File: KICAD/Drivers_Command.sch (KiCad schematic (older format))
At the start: 12 parts

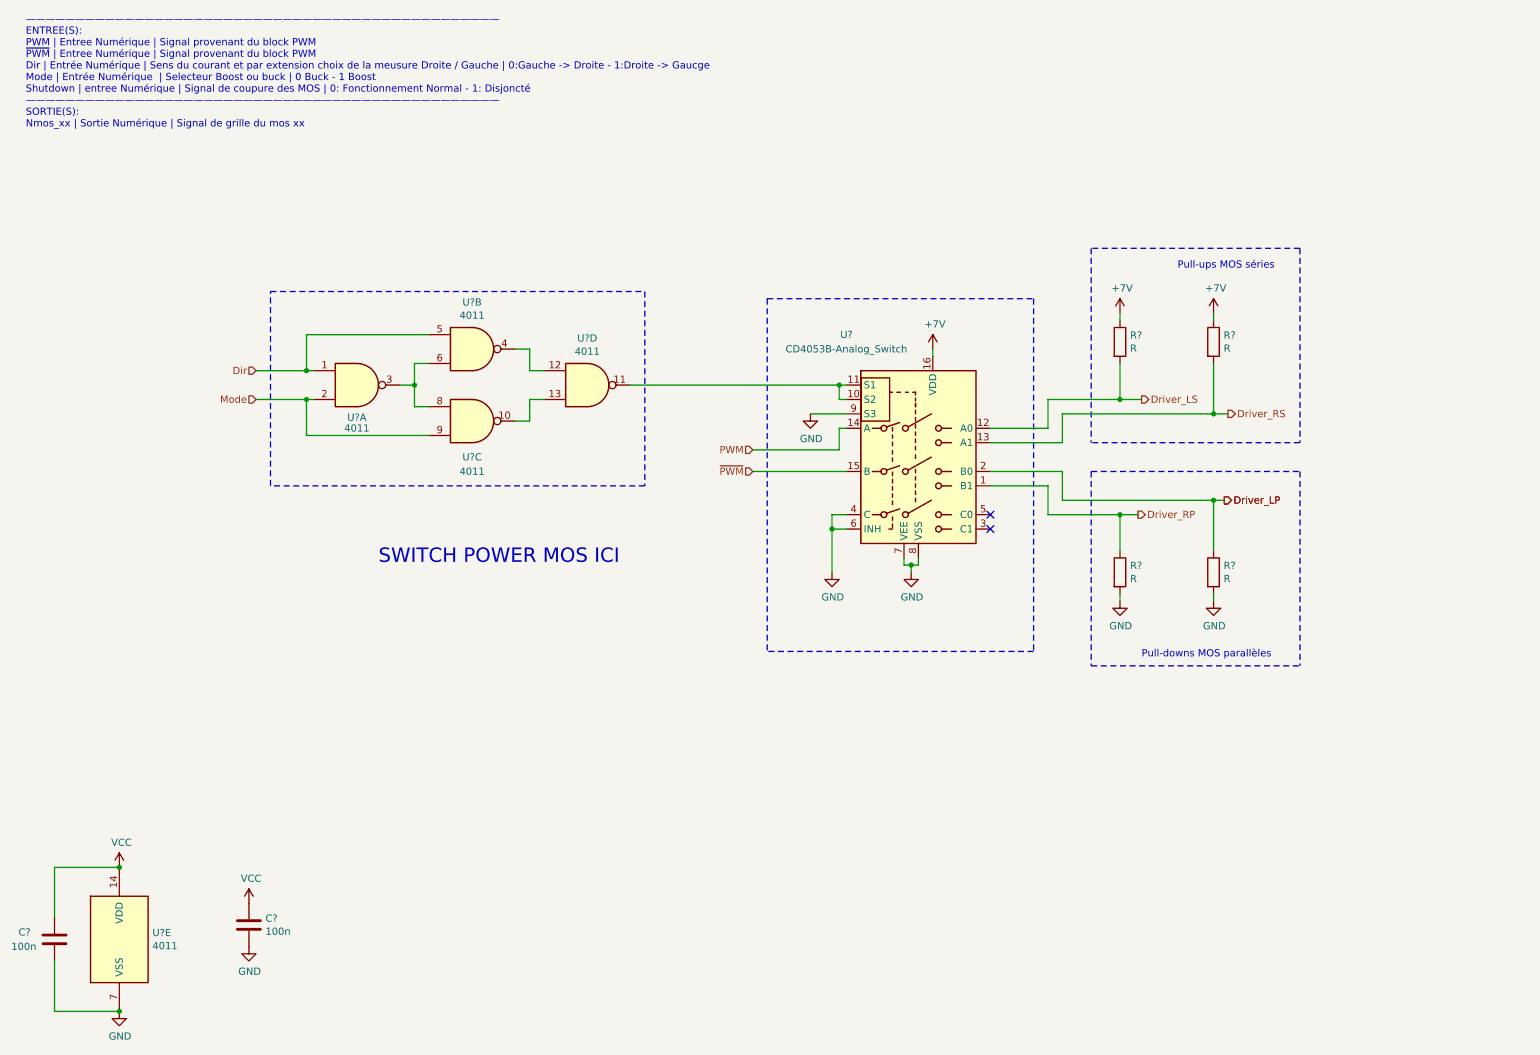
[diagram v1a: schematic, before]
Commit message: reworked driver command
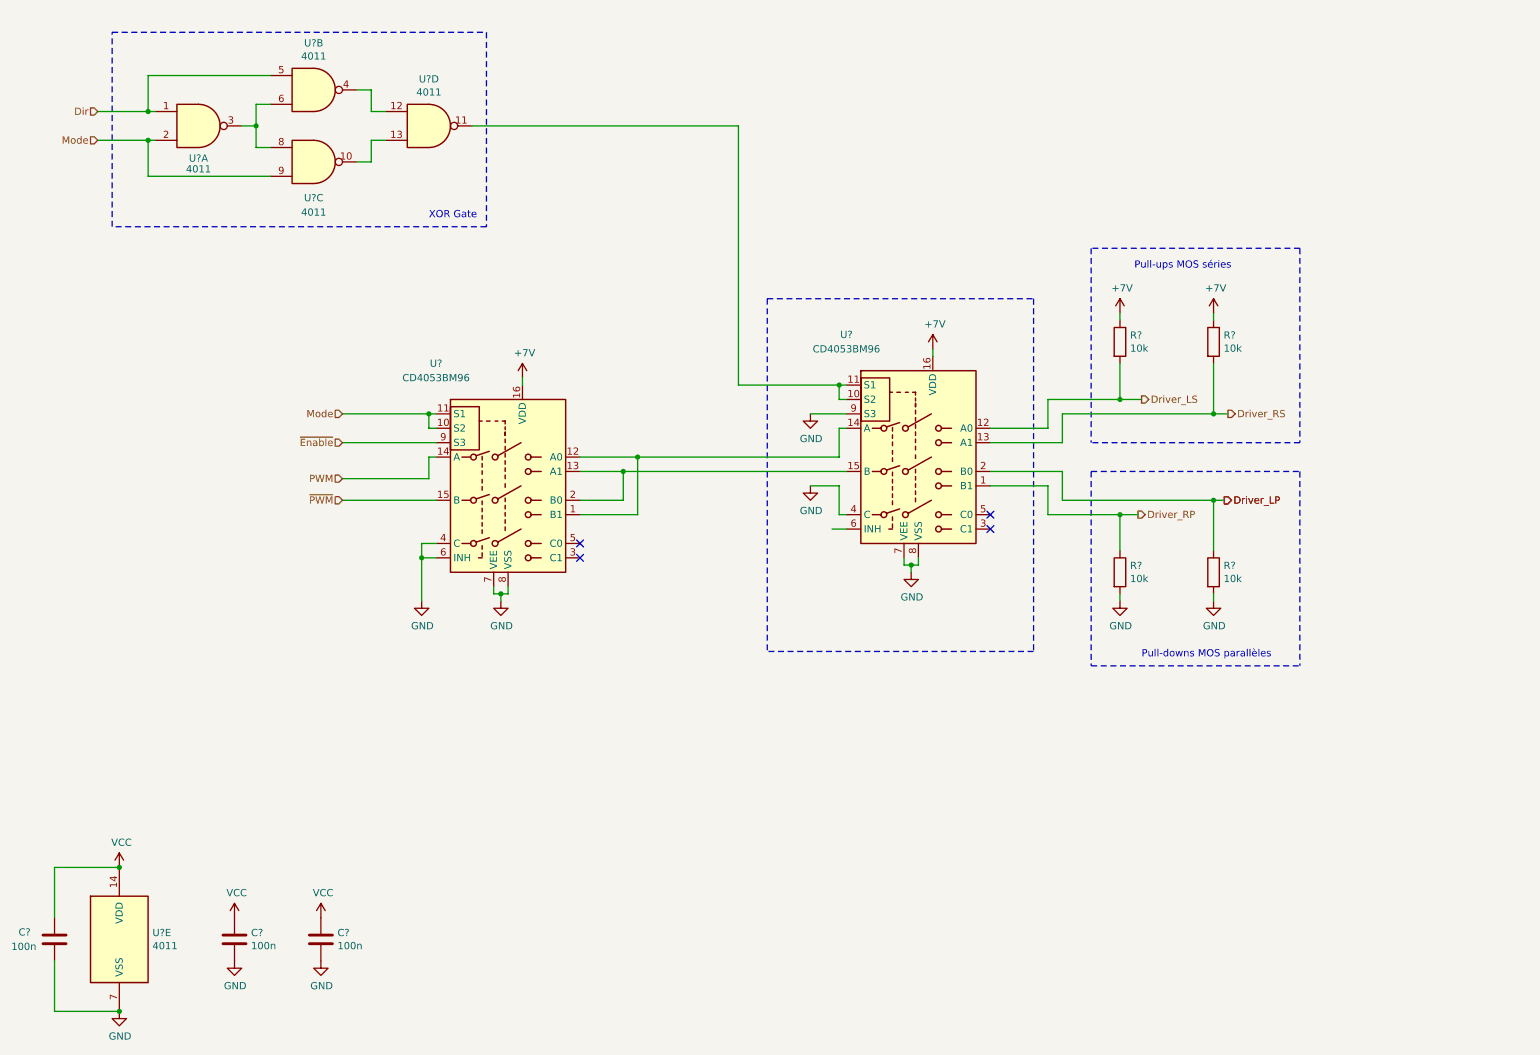
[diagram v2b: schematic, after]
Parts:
- removed R? (x3): R, symbol Device:R
- added C?: 100n, Capacitor_SMD:C_0805_2012Metric_Pad1.15x1.40mm_HandSolder, symbol Device:C
- added R? (x3): 10k, Resistor_SMD:R_0805_2012Metric_Pad1.15x1.40mm_HandSolder, symbol Device:R
- added U?: CD4053BM96, Package_SO:SO-16_3.9x9.9mm_P1.27mm, symbol sesame-fonctionnel-rescue:CD4053B-Analog_Switch
- C? (x2): footprint (none) -> Capacitor_SMD:C_0805_2012Metric_Pad1.15x1.40mm_HandSolder
- R?: value R -> 10k; footprint (none) -> Resistor_SMD:R_0805_2012Metric_Pad1.15x1.40mm_HandSolder
- U?: value CD4053B-Analog_Switch -> CD4053BM96; footprint (none) -> Package_SO:SO-16_3.9x9.9mm_P1.27mm
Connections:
- net +7V: now also R?.1, U?.16 (VDD)
- net Driver_LP: now also R?.1
- net Driver_LS: now also R?.2
- net Driver_RP: now also R?.1
- net GND: now also C?.2, R?.2, R?.2, U?.4 (C), U?.6 (INH), U?.7 (VEE), U?.8 (VSS); no longer U?.6 (INH)
- net Mode: now also U?.10 (S2), U?.11 (S1)
- net PWM: now also U?.14 (A); no longer U?.14 (A)
- net VCC: now also C?.1
- net ~PWM: now also U?.15 (B); no longer U?.15 (B)
- new net: U?.1 (B1), U?.12 (A0), U?.14 (A)
- new net: U?.13 (A1), U?.15 (B), U?.2 (B0)
- new net ~Enable: U?.9 (S3)
- no-connect marks 2 -> 4
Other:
- note added: "XOR Gate"
- note removed: "SWITCH POWER MOS ICI"
- note removed: "————————————————————————————————————————————————\nENTREE(S):\nPWM | Entree Numérique | Signal provenant du block PWM\n~PWM~ | Entree Numérique | Signal provenant du block PWM\nDir | Entrée Numérique | Sens du courant et par extension choix de la meusure Droite / Gauche | 0:Gauche -> Droite - 1:Droite -> Gaucge\nMode | Entrée Numérique | Selecteur Boost ou buck | 0 Buck - 1 Boost\nShutdown | entre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"
- moved on the sheet: C?, U?A, U?B, U?C, U?D

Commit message: worked on power supply + connectors
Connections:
- net +7V: no longer R?.1, R?.1
- net GND: now also U?.3 (C1); no longer U?.4 (C)
- net VCC: now also U?.5 (C0)
- net ~Enable: now also U?.6 (INH)
- new net Resistor_pull: R?.1, R?.1, U?.4 (C)
- no-connect marks 4 -> 2
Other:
- note added: "Pull-down MOS in parallel"
- note added: "Pull-up/down MOS in series"
- note added: "inverser A et C pour le pinout ?"
- note removed: "Pull-downs MOS parallèles"
- note removed: "Pull-ups MOS séries"
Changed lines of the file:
@@
 PWM
-Wire Wire Line
-	6250 4150 6350 4150
 Wire Wire Line
 	6350 3250 6300 3250
@@
 Wire Notes Line
 	8050 3750 9500 3750
-Text Notes 8350 2350 0    50   ~ 0
-Pull-ups MOS séries
+Text Notes 8250 2350 0    50   ~ 0
+Pull-up/down MOS in series
 Wire Notes Line
 	9500 2200 8050 2200
@@
 Wire Notes Line
 	8050 3750 8050 5100
-Text Notes 8400 5050 0    50   ~ 0
-Pull-downs MOS parallèles
+Text Notes 8300 5050 0    50   ~ 0
+Pull-down MOS in parallel
 Wire Wire Line
 	6300 3150 6300 3250
@@
 L power:GND #PWR?
 U 1 1 613BCF5A
-P 3400 4650
-F 0 "#PWR?" H 3400 4400 50  0001 C CNN
-F 1 "GND" H 3405 4477 50  0000 C CNN
-F 2 "" H 3400 4650 50  0001 C CNN
-F 3 "" H 3400 4650 50  0001 C CNN
-	1    3400 4650
-	1    0    0    -1
-$EndComp
-Wire Wire Line
-	3400 4650 3400 4350
+P 3400 4450
+F 0 "#PWR?" H 3400 4200 50  0001 C CNN
+F 1 "GND" H 3405 4277 50  0000 C CNN
+F 2 "" H 3400 4450 50  0001 C CNN
+F 3 "" H 3400 4450 50  0001 C CNN
+	1    3400 4450
+	1    0    0    -1
+$EndComp
+Wire Wire Line
+	3400 4450 3400 4350
 Wire Wire Line
 	3500 3450 3450 3450
 Wire Wire Line
 	3450 3350 3500 3350
-NoConn ~ 4500 4250
-NoConn ~ 4500 4350
 Wire Wire Line
 	4100 3100 4100 3150
@@
 	2850 3950 3500 3950
 Wire Wire Line
-	4500 3950 4800 3950
-Wire Wire Line
-	4500 4050 4900 4050
-Wire Wire Line
-	4500 3650 4900 3650
-Wire Wire Line
-	4500 3750 4800 3750
+	4500 3950 4550 3950
+Wire Wire Line
+	4500 4050 4650 4050
 Wire Wire Line
 	3450 3350 3450 3450
@@
 Wire Wire Line
 	3450 3650 3450 3800
-Wire Wire Line
-	3500 4250 3400 4250
-Wire Wire Line
-	3400 4250 3400 4350
-Connection ~ 3400 4350
 $Comp
 L Sesame:+7V #PWR?
@@
 	3450 3350 2850 3350
 Connection ~ 3450 3350
-Wire Wire Line
-	4900 3650 4900 4050
-Wire Wire Line
-	4800 3750 4800 3950
-Wire Wire Line
-	4900 3650 6300 3650
-Connection ~ 4900 3650
-Wire Wire Line
-	4800 3750 6350 3750
-Connection ~ 4800 3750
 Wire Wire Line
 	3750 1350 5600 1350
@@
 	1    0    0    -1
 $EndComp
-$Comp
-L Sesame:+7V #PWR?
-U 1 1 61441A17
-P 8250 2650
-F 0 "#PWR?" H 8250 2500 50  0001 C CNN
-F 1 "+7V" H 8265 2823 50  0000 C CNN
-F 2 "" H 8250 2650 50  0001 C CNN
-F 3 "" H 8250 2650 50  0001 C CNN
-	1    8250 2650
-	1    0    0    -1
-$EndComp
-$Comp
-L Sesame:+7V #PWR?
-U 1 1 614442E1
-P 8900 2650
-F 0 "#PWR?" H 8900 2500 50  0001 C CNN
-F 1 "+7V" H 8915 2823 50  0000 C CNN
-F 2 "" H 8900 2650 50  0001 C CNN
-F 3 "" H 8900 2650 50  0001 C CNN
-	1    8900 2650
-	1    0    0    -1
-$EndComp
 Text Notes 3450 2000 0    50   ~ 0
 XOR Gate
@@
 L power:GND #PWR?
 U 1 1 61454AC0
-P 6100 3850
-F 0 "#PWR?" H 6100 3600 50  0001 C CNN
-F 1 "GND" H 6105 3677 50  0000 C CNN
-F 2 "" H 6100 3850 50  0001 C CNN
-F 3 "" H 6100 3850 50  0001 C CNN
-	1    6100 3850
-	1    0    0    -1
-$EndComp
-Wire Wire Line
-	6100 3850 6300 3850
-Wire Wire Line
-	6300 3850 6300 4050
+P 6100 3800
+F 0 "#PWR?" H 6100 3550 50  0001 C CNN
+F 1 "GND" H 6105 3627 50  0000 C CNN
+F 2 "" H 6100 3800 50  0001 C CNN
+F 3 "" H 6100 3800 50  0001 C CNN
+	1    6100 3800
+	1    0    0    -1
+$EndComp
+Wire Wire Line
+	6100 3800 6300 3800
+Wire Wire Line
+	6300 3800 6300 4050
 Wire Wire Line
 	6300 4050 6350 4050
@@
 	1    0    0    -1
 $EndComp
+Text Label 2950 3550 0    50   ~ 0
+~Enable
+Wire Wire Line
+	6000 4150 6350 4150
+Text Label 6000 4150 0    50   ~ 0
+~Enable
+Text Label 2900 4250 0    50   ~ 0
+Resistor_pull
+Wire Wire Line
+	3500 4250 2900 4250
+$Comp
+L power:GND #PWR?
+U 1 1 6130709D
+P 4800 4400
+F 0 "#PWR?" H 4800 4150 50  0001 C CNN
+F 1 "GND" H 4805 4227 50  0000 C CNN
+F 2 "" H 4800 4400 50  0001 C CNN
+F 3 "" H 4800 4400 50  0001 C CNN
+	1    4800 4400
+	1    0    0    -1
+$EndComp
+Wire Wire Line
+	4800 4400 4800 4350
+Wire Wire Line
+	8250 2650 8900 2650
+Text Label 8350 2650 0    50   ~ 0
+Resistor_pull
+Wire Wire Line
+	4800 4350 4500 4350
+$Comp
+L power:VCC #PWR?
+U 1 1 61311635
+P 4800 4200
+F 0 "#PWR?" H 4800 4050 50  0001 C CNN
+F 1 "VCC" H 4815 4373 50  0000 C CNN
+F 2 "" H 4800 4200 50  0001 C CNN
+F 3 "" H 4800 4200 50  0001 C CNN
+	1    4800 4200
+	1    0    0    -1
+$EndComp
+Wire Wire Line
+	4500 4250 4800 4250
+Wire Wire Line
+	4800 4250 4800 4200
+Wire Wire Line
+	4500 3750 4550 3750
+Wire Wire Line
+	4500 3650 4650 3650
+Wire Wire Line
+	4550 3950 4550 3750
+Connection ~ 4550 3750
+Wire Wire Line
+	4550 3750 6350 3750
+Wire Wire Line
+	4650 4050 4650 3650
+Connection ~ 4650 3650
+Wire Wire Line
+	4650 3650 6300 3650
+Text Notes 2800 5050 0    100  ~ 0
+inverser A et C pour le pinout ?
 $EndSCHEMATC

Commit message: mainly footprints
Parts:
- gave numbers to parts that had none: 3
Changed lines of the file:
@@
 $Descr A4 11693 8268
 encoding utf-8
-Sheet 12 16
+Sheet 7 16
 Title "SESAME"
 Date "2021-08-04"
@@
 	850  6500 850  6850
 $Comp
-L 4xxx:4011 U?
+L 4xxx:4011 U6
 U 5 1 610DDCAD
 P 1300 7000
-F 0 "U?" H 1530 7046 50  0000 L CNN
+F 0 "U6" H 1530 7046 50  0000 L CNN
 F 1 "4011" H 1530 6955 50  0000 L CNN
 F 2 "" H 1300 7000 50  0001 C CNN
@@
 ~Enable
 $Comp
-L sesame-fonctionnel-rescue:CD4053B-Analog_Switch U?
+L sesame-fonctionnel-rescue:CD4053B-Analog_Switch U5
 U 1 1 610F7E61
 P 6850 3650
-F 0 "U?" H 6350 4500 50  0000 C CNN
+F 0 "U5" H 6350 4500 50  0000 C CNN
 F 1 "CD4053BM96" H 6350 4400 50  0000 C CNN
 F 2 "Package_SO:SO-16_3.9x9.9mm_P1.27mm" H 7000 2900 50  0001 L CNN
@@
 $EndComp
 $Comp
-L sesame-fonctionnel-rescue:CD4053B-Analog_Switch U?
+L sesame-fonctionnel-rescue:CD4053B-Analog_Switch U4
 U 1 1 613BCF53
 P 4000 3850
-F 0 "U?" H 3500 4700 50  0000 C CNN
+F 0 "U4" H 3500 4700 50  0000 C CNN
 F 1 "CD4053BM96" H 3500 4600 50  0000 C CNN
 F 2 "Package_SO:SO-16_3.9x9.9mm_P1.27mm" H 4150 3100 50  0001 L CNN
@@
 $EndComp
 $Comp
-L 4xxx:4011 U?
+L 4xxx:4011 U6
 U 3 1 6119334A
 P 2650 1600
-F 0 "U?" H 2650 1350 50  0000 C CNN
+F 0 "U6" H 2650 1350 50  0000 C CNN
 F 1 "4011" H 2650 1250 50  0000 C CNN
 F 2 "" H 2650 1600 50  0001 C CNN
@@
 $EndComp
 $Comp
-L 4xxx:4011 U?
+L 4xxx:4011 U6
 U 4 1 6119F84F
 P 3450 1350
-F 0 "U?" H 3450 1675 50  0000 C CNN
+F 0 "U6" H 3450 1675 50  0000 C CNN
 F 1 "4011" H 3450 1584 50  0000 C CNN
 F 2 "" H 3450 1350 50  0001 C CNN
@@
 $EndComp
 $Comp
-L 4xxx:4011 U?
+L 4xxx:4011 U6
 U 1 1 61192492
 P 1850 1350
-F 0 "U?" H 1850 1125 50  0000 C CNN
+F 0 "U6" H 1850 1125 50  0000 C CNN
 F 1 "4011" H 1850 1050 50  0000 C CNN
 F 2 "" H 1850 1350 50  0001 C CNN
@@
 $EndComp
 $Comp
-L 4xxx:4011 U?
+L 4xxx:4011 U6
 U 2 1 61194533
 P 2650 1100
-F 0 "U?" H 2650 1425 50  0000 C CNN
+F 0 "U6" H 2650 1425 50  0000 C CNN
 F 1 "4011" H 2650 1334 50  0000 C CNN
 F 2 "" H 2650 1100 50  0001 C CNN

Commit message: revex with jmt
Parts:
- added R? (x2): NC, Resistor_SMD:R_0805_2012Metric_Pad1.15x1.40mm_HandSolder, symbol Device:R
- added R?: 10k, Resistor_SMD:R_0805_2012Metric_Pad1.15x1.40mm_HandSolder, symbol Device:R
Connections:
- net GND: now also R?.2, R?.2, R?.2; no longer U5.4 (C)
- net Dir_Xor_Mode: now reaches U5.10 (S2), U5.11 (S1), U6.11
- net at U5.3 (C1): now also R?.1
- net at U5.5 (C0): now also R?.1
- new net: R?.1, U5.4 (C)
- no-connect marks 2 -> 0
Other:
- note added: "Don’t populate"
- moved on the sheet: R?

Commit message: minor cleanup
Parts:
- added R?: 10k, Resistor_SMD:R_0805_2012Metric_Pad1.15x1.40mm_HandSolder, symbol Device:R
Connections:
- net +7V is gone; now on net VCC: U4.16 (VDD), U5.16 (VDD)
- net GND: now also R?.1; no longer U5.9 (S3)
- new net: R?.2, U5.9 (S3)
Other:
- moved on the sheet: U4, U6A, U6B, U6C, U6D
